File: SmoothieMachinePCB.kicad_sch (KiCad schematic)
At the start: 49 parts, among them J1 Up Button, J10 Vin, J2 Down Button, J3 Next Ingredient Button, J4 Next Recipe Button, J5 Solenoid Valve, J6 Conn_01x16_Socket, J7 10KPOT, J8 Stepper Motor, J9 LoadCell, U1 ESP32-S3-WROOM-2, U2 LM1117MP-3.3, U3 DRV8825PWP, U4 VN10KN3-G, U5 LM1117MP-5.0, U6 NAU7802SGI

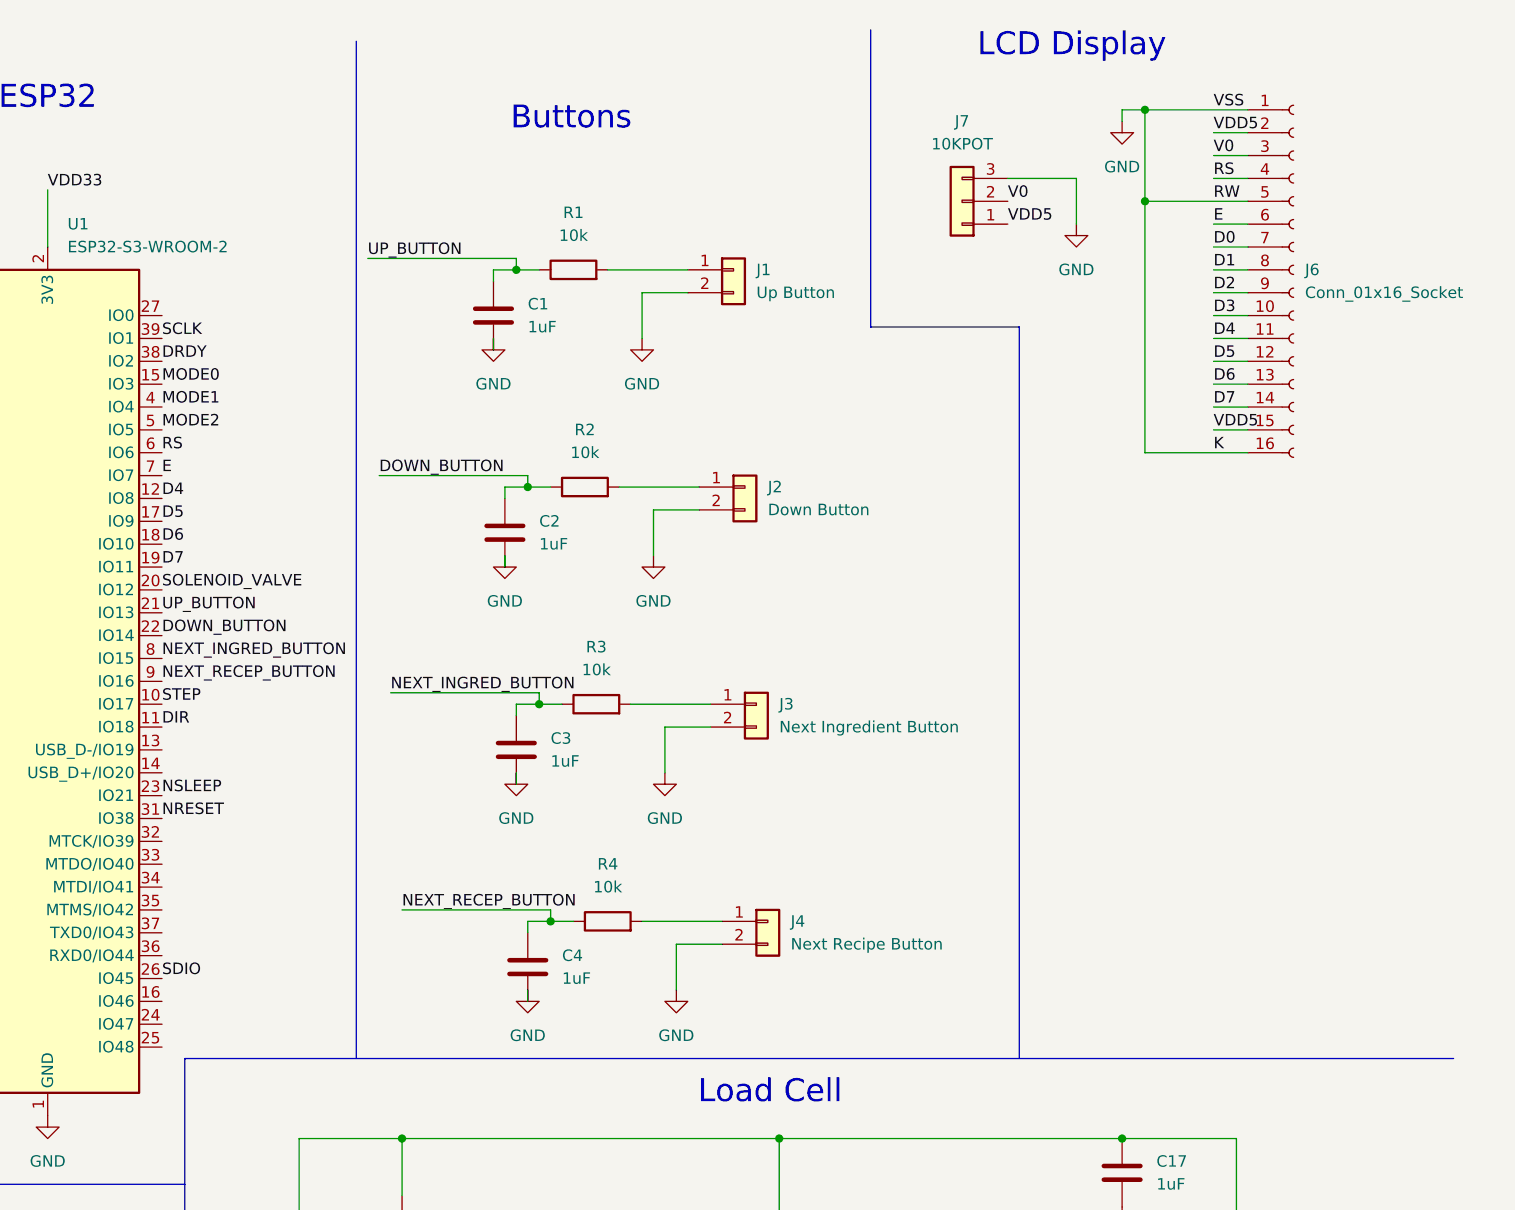
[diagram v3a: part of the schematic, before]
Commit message: Changed LCD Display to 1x4 connector, removed debouncing circuits, and added mounting holes
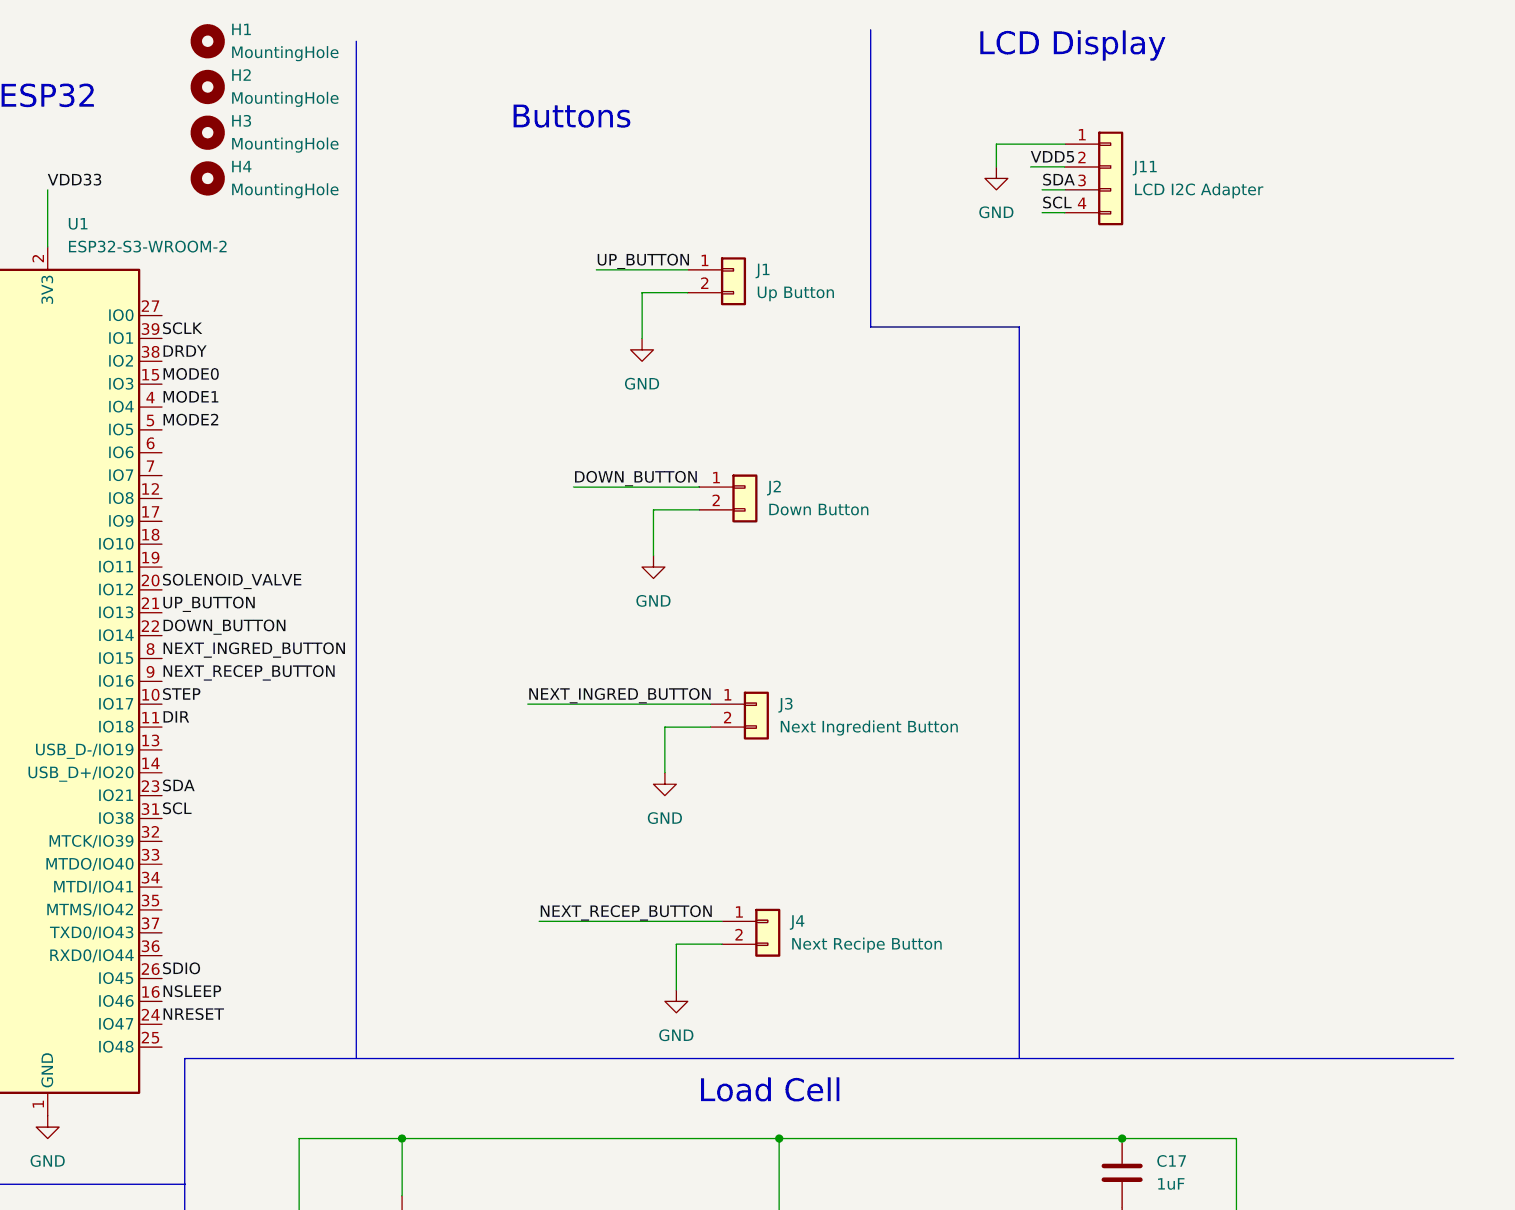
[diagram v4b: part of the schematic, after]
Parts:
- removed C1, C2, C3, C4: 1uF, symbol Device:C
- removed J6: Conn_01x16_Socket, symbol Connector:Conn_01x16_Socket
- removed J7: 10KPOT, symbol Connector_Generic:Conn_01x03
- removed R1, R2, R3, R4: 10k, symbol Device:R
- added H1, H2, H3, H4: MountingHole, symbol Mechanical:MountingHole
- added J11: LCD I2C Adapter, symbol Connector_Generic:Conn_01x04
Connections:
- net DOWN_BUTTON: now also J2.1 (Pin_1)
- net GND: now also J11.1 (Pin_1)
- net NEXT_INGRED_BUTTON: now also J3.1 (Pin_1)
- net NEXT_RECEP_BUTTON: now also J4.1 (Pin_1)
- net NRESET: now also U1.24 (IO47); no longer U1.31 (IO38)
- net NSLEEP: now also U1.16 (IO46); no longer U1.23 (IO21)
- net UP_BUTTON: now also J1.1 (Pin_1)
- net VDD5: now also J11.2 (Pin_2)
- net D4: no longer names the net of U1.12 (IO8)
- net D5: no longer names the net of U1.17 (IO9)
- net D6: no longer names the net of U1.18 (IO10)
- net D7: no longer names the net of U1.19 (IO11)
- net E: no longer names the net of U1.7 (IO7)
- net RS: no longer names the net of U1.6 (IO6)
- new net SCL: J11.4 (Pin_4), U1.31 (IO38)
- new net SDA: J11.3 (Pin_3), U1.23 (IO21)

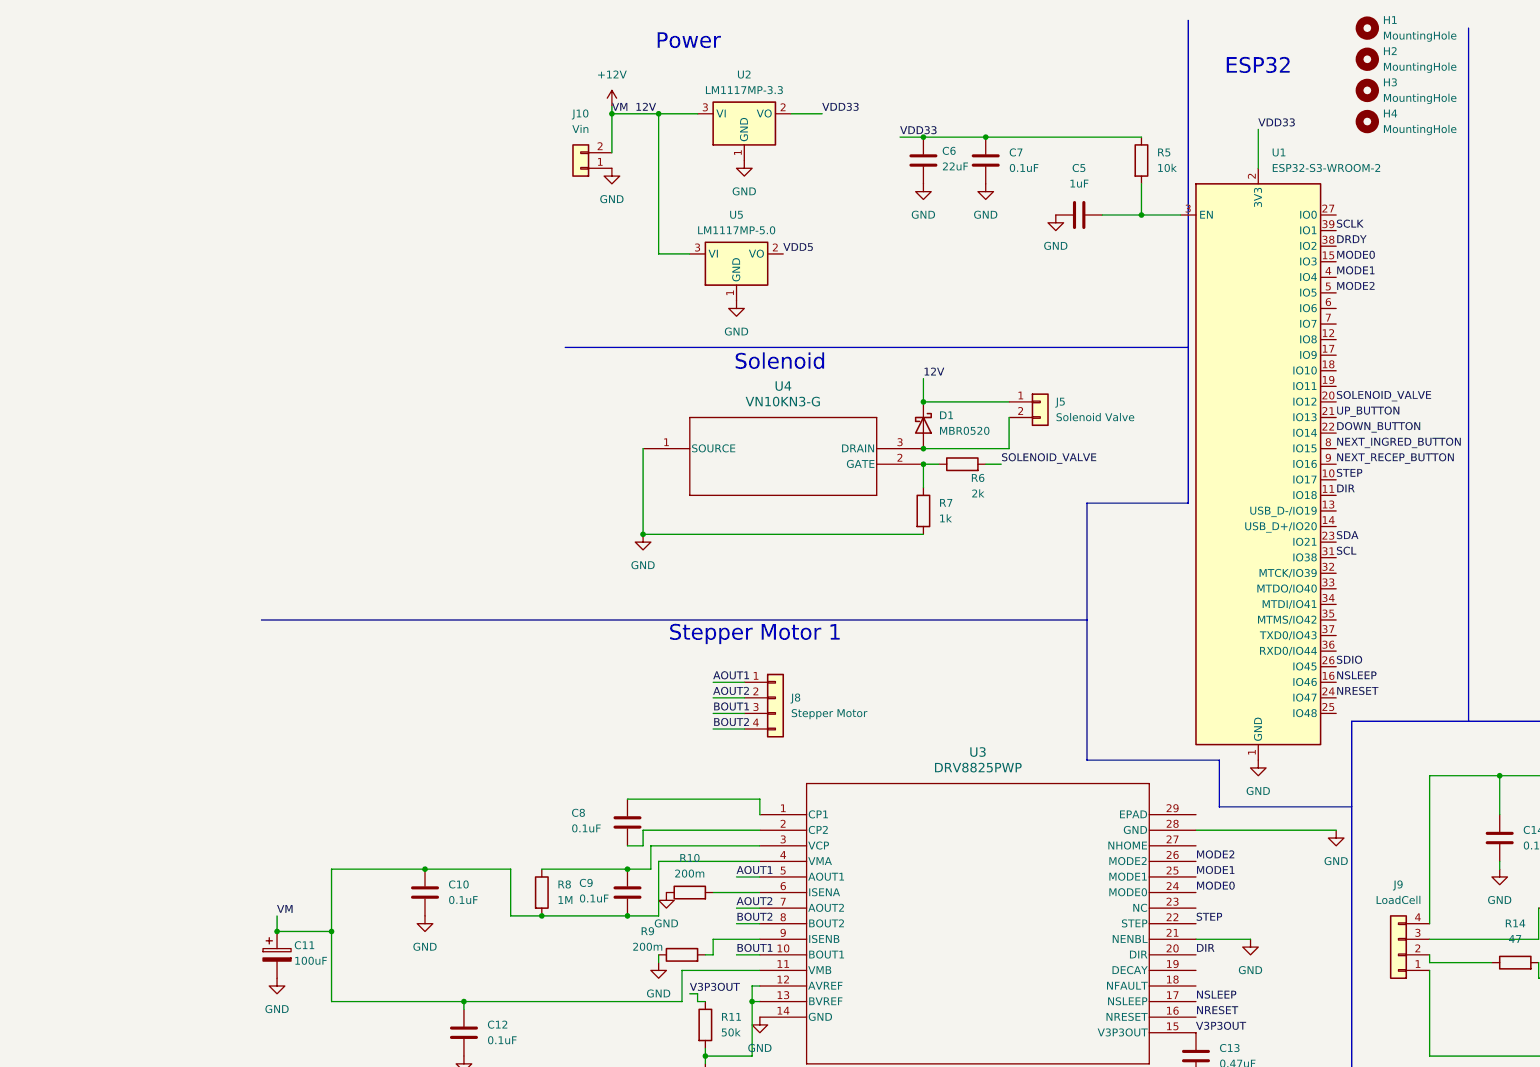
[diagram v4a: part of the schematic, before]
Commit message: Finished footprint assignments, have to place and route
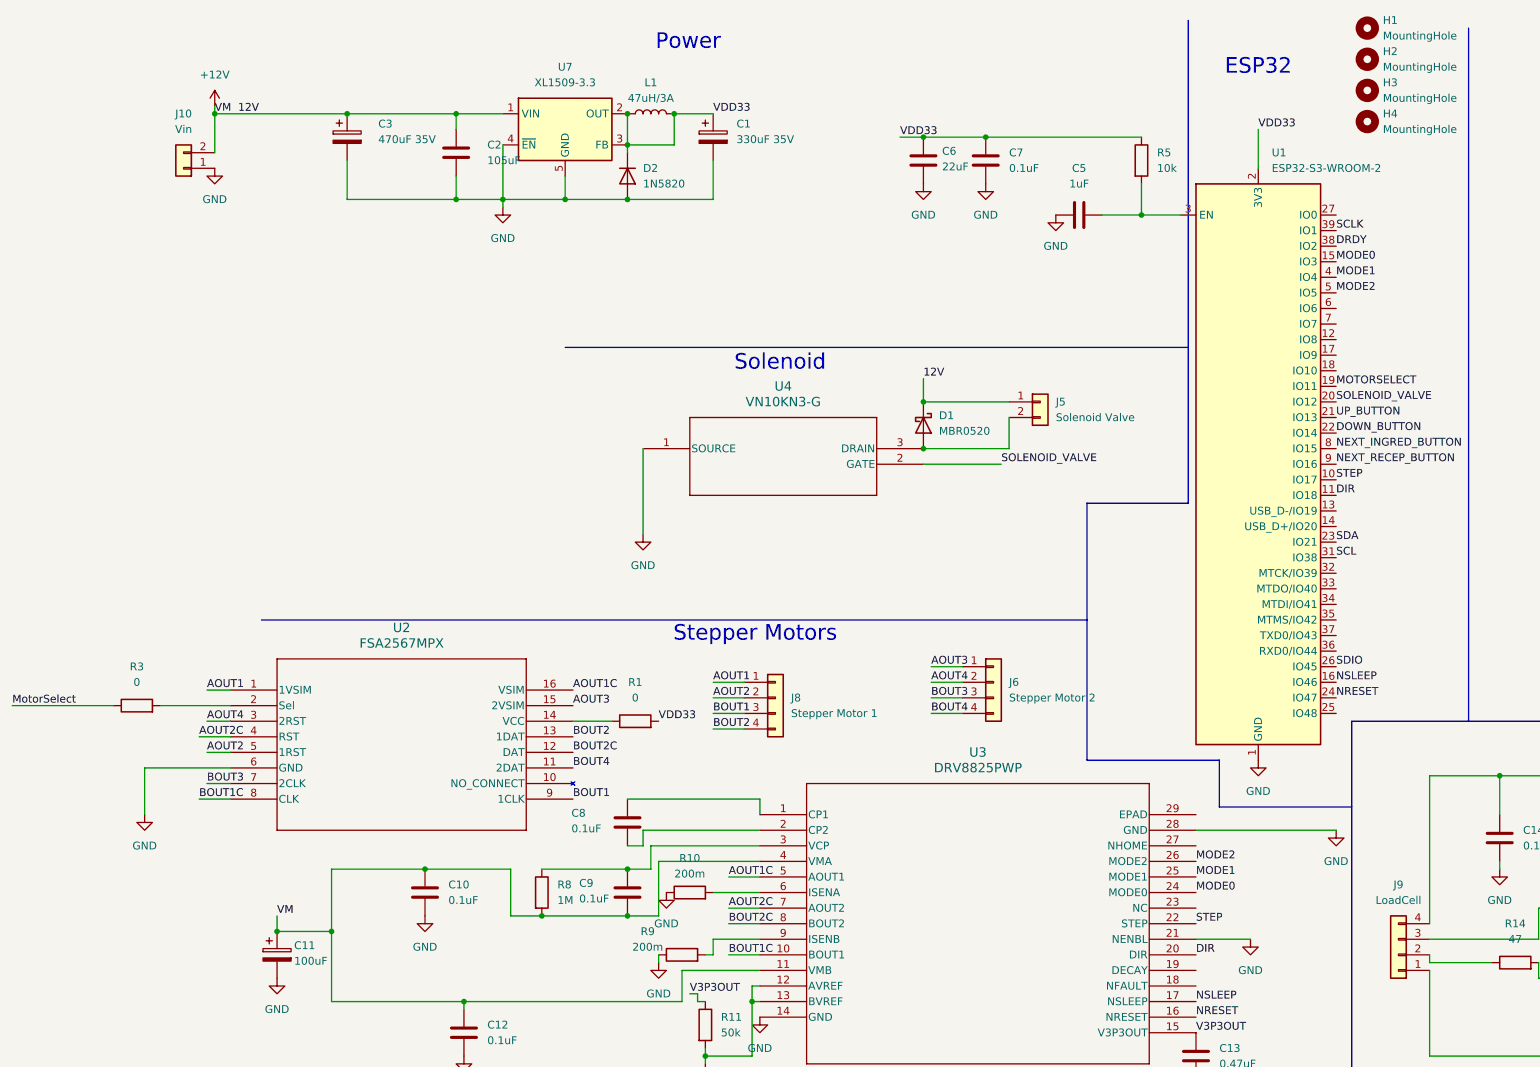
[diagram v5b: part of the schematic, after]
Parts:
- removed R6: 2k, symbol Device:R
- removed R7: 1k, symbol Device:R
- removed U2: LM1117MP-3.3, Package_TO_SOT_SMD:SOT-223-3_TabPin2, symbol Regulator_Linear:LM1117MP-3.3
- removed U5: LM1117MP-5.0, Package_TO_SOT_SMD:SOT-223-3_TabPin2, symbol Regulator_Linear:LM1117MP-5.0
- added C1: 330uF 35V, Capacitor_SMD:CP_Elec_10x12.5, symbol Device:C_Polarized
- added C2: 105uF, Capacitor_SMD:C_0805_2012Metric_Pad1.18x1.45mm_HandSolder, symbol Device:C
- added C3: 470uF 35V, UUJ1V471MNJ6MS:CAP_UUG_12P5X21_NCH, symbol Device:C_Polarized
- added D2: 1N5820, 1N5820:CR_0-E3&slash_54_VIS, symbol Device:D
- added J6: Stepper Motor 2, Connector_Molex:Molex_KK-254_AE-6410-04A_1x04_P2.54mm_Vertical, symbol Connector_Generic:Conn_01x04
- added L1: 47uH/3A, Inductor_SMD:L_0805_2012Metric_Pad1.05x1.20mm_HandSolder, symbol Device:L
- added R1, R3: 0, Resistor_SMD:R_0805_2012Metric_Pad1.20x1.40mm_HandSolder, symbol Device:R
- added U2: FSA2567MPX, FSA2567MPX:UMLP16_1P8X2P6_ONS, symbol FSA2567MPX:FSA2567MPX
- added U7: XL1509-3.3, Package_SO:SOIC-8_3.9x4.9mm_P1.27mm, symbol Regulator_Switching:XL1509-3.3
- C10, C11, C12, C13, C14, C15, C16, C17, C18, C5, C6, C7, C8, C9: footprint (none) -> Capacitor_SMD:C_0805_2012Metric_Pad1.18x1.45mm_HandSolder
- H1, H2, H3, H4: footprint (none) -> MountingHole:MountingHole_3.2mm_M3
- J1, J10, J2, J3, J4, J5: footprint (none) -> Connector_Molex:Molex_KK-254_AE-6410-02A_1x02_P2.54mm_Vertical
- J11, J9: footprint (none) -> Connector_Molex:Molex_KK-254_AE-6410-04A_1x04_P2.54mm_Vertical
- J8: value Stepper Motor -> Stepper Motor 1; footprint (none) -> Connector_Molex:Molex_KK-254_AE-6410-04A_1x04_P2.54mm_Vertical
- R10, R11, R12, R13, R14, R5, R8, R9: footprint (none) -> Resistor_SMD:R_0805_2012Metric_Pad1.20x1.40mm_HandSolder
- U3: footprint PWP28_5P18X3P1 -> DRV8825PWP:PWP28_5P18X3P1
- U4: footprint TO-92_MC_MCH -> VN10KN3-G:TO-92_MC_MCH
- U6: footprint SOI16_NAU7802SGI_NUV -> NAU7802SGI:SOI16_NAU7802SGI_NUV
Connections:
- net +12V: now also C2.1, C3.1, U7.1 (VIN)
- net AOUT1: now also U2.1 (1VSIM); no longer U3.5 (AOUT1)
- net AOUT2: now also U2.5 (1RST); no longer U3.7 (AOUT2)
- net BOUT1: now also U2.9 (1CLK); no longer U3.10 (BOUT1)
- net BOUT2: now also U2.13 (1DAT); no longer U3.8 (BOUT2)
- net GND: now also C1.2, C2.2, C3.2, D2.2 (A), U2.6 (GND), U7.4 (~{EN}), U7.5 (GND), U7.6 (GND), U7.7 (GND), U7.8 (GND)
- net SOLENOID_VALVE: now also U4.2 (GATE)
- net VDD33: now also C1.1, D2.1 (K), L1.1, L1.2, R1.2, U7.2 (OUT), U7.3 (FB)
- net MOTORSELECT: now reaches U1.19 (IO11)
- new net: R3.2, U2.2 (Sel)
- new net: R1.1, U2.14 (VCC)
- new net AOUT1C: U2.16 (VSIM), U3.5 (AOUT1)
- new net AOUT2C: U2.4 (RST), U3.7 (AOUT2)
- new net AOUT3: J6.1 (Pin_1), U2.15 (2VSIM)
- new net AOUT4: J6.2 (Pin_2), U2.3 (2RST)
- new net BOUT1C: U2.8 (CLK), U3.10 (BOUT1)
- new net BOUT2C: U2.12 (DAT), U3.8 (BOUT2)
- new net BOUT3: J6.3 (Pin_3), U2.7 (2CLK)
- new net BOUT4: J6.4 (Pin_4), U2.11 (2DAT)
- new net MotorSelect: R3.1
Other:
- note added: "Stepper Motors"
- note removed: "Stepper Motor 1"
- moved on the sheet: J10

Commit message: Second round pcb files
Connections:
- net MotorSelect is gone; now on net MOTORSELECT: R3.1
- net VDD5 is gone; now on net VDD33: J11.2 (Pin_2)
- net VDD33: no longer D2.1 (K), L1.1, U7.2 (OUT)
- new net: D2.1 (K), L1.1, U7.2 (OUT)
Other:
- moved on the sheet: D2
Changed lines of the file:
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@@
 	)
 	(junction
-		(at 22.86 34.29)
-		(diameter 0)
-		(color 0 0 0 0)
-	)
-	(junction
 		(at 35.56 182.88)
 		(diameter 0)
@@
 	)
 	(junction
-		(at 22.86 43.18)
-		(diameter 0)
-		(color 0 0 0 0)
-	)
-	(junction
 		(at 245.11 137.16)
 		(diameter 0)
@@
 	)
 	(junction
+		(at 36.83 43.18)
+		(diameter 0)
+		(color 0 0 0 0)
+	)
+	(junction
 		(at 8.89 160.02)
 		(diameter 0)
@@
 	(wire
 		(pts
-			(xy 36.83 43.18) (xy 22.86 43.18)
+			(xy 22.86 21.59) (xy 22.86 29.21)
 		)
 		(stroke
@@
 	(wire
 		(pts
-			(xy 234.95 29.21) (xy 238.76 29.21)
+			(xy 233.68 29.21) (xy 238.76 29.21)
 		)
 		(stroke
@@
 	(wire
 		(pts
-			(xy 22.86 34.29) (xy 22.86 29.21)
-		)
-		(stroke
-			(width 0)
-			(type default)
-		)
-	)
-	(wire
-		(pts
 			(xy 44.45 151.13) (xy 27.94 151.13)
 		)
@@
 	(wire
 		(pts
-			(xy 12.7 43.18) (xy 22.86 43.18)
+			(xy 12.7 43.18) (xy 36.83 43.18)
 		)
 		(stroke
@@
 	(wire
 		(pts
+			(xy 53.34 29.21) (xy 53.34 43.18)
+		)
+		(stroke
+			(width 0)
+			(type default)
+		)
+	)
+	(wire
+		(pts
 			(xy -41.91 135.89) (xy -55.88 135.89)
 		)
@@
 	(wire
 		(pts
+			(xy 53.34 43.18) (xy 36.83 43.18)
+		)
+		(stroke
+			(width 0)
+			(type default)
+		)
+	)
+	(wire
+		(pts
 			(xy -25.4 162.56) (xy -25.4 173.99)
 		)
@@
 	(wire
 		(pts
-			(xy 22.86 35.56) (xy 22.86 34.29)
+			(xy 53.34 21.59) (xy 22.86 21.59)
 		)
 		(stroke
@@
 		)
 	)
-	(label "MotorSelect"
+	(label "MOTORSELECT"
 		(at -77.47 125.73 0)
 		(effects
@@
 		)
 	)
-	(label "VDD5"
-		(at 234.95 29.21 0)
-		(effects
-			(font
-				(size 1.27 1.27)
-			)
-			(justify left bottom)
-		)
-	)
 	(label "AOUT4"
 		(at -45.72 128.27 0)
@@
 		)
 	)
+	(label "VDD33"
+		(at 233.68 29.21 0)
+		(effects
+			(font
+				(size 1.27 1.27)
+			)
+			(justify left bottom)
+		)
+	)
 	(label "SCLK"
 		(at 257.81 163.83 0)
@@
 	(symbol
 		(lib_id "Device:D")
-		(at 22.86 39.37 270)
+		(at 53.34 25.4 270)
 		(unit 1)
 		(exclude_from_sim no)
@@
 		(fields_autoplaced yes)
 		(property "Reference" "D2"
-			(at 25.4 38.0999 90)
+			(at 55.88 24.1299 90)
 			(effects
 				(font
@@
 		)
 		(property "Value" "1N5820"
-			(at 25.4 40.6399 90)
+			(at 55.88 26.6699 90)
 			(effects
 				(font
@@
 		)
 		(property "Footprint" "1N5820:CR_0-E3&slash_54_VIS"
-			(at 22.86 39.37 0)
+			(at 53.34 25.4 0)
 			(effects
 				(font
@@
 		)
 		(property "Datasheet" "~"
-			(at 22.86 39.37 0)
+			(at 53.34 25.4 0)
 			(effects
 				(font
@@
 		)
 		(property "Description" "Diode"
-			(at 22.86 39.37 0)
+			(at 53.34 25.4 0)
 			(effects
 				(font
@@
 		)
 		(property "Sim.Device" "D"
-			(at 22.86 39.37 0)
+			(at 53.34 25.4 0)
 			(effects
 				(font
@@
 		)
 		(property "Sim.Pins" "1=K 2=A"
-			(at 22.86 39.37 0)
+			(at 53.34 25.4 0)
 			(effects
 				(font
